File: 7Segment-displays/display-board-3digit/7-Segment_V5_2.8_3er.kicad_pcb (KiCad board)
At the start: 2 copper layers, 47.8 x 10.7 mm, 5 parts, among them J1 Conn_02x08_Odd_Even, U1 7Segment 3 digit common catho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

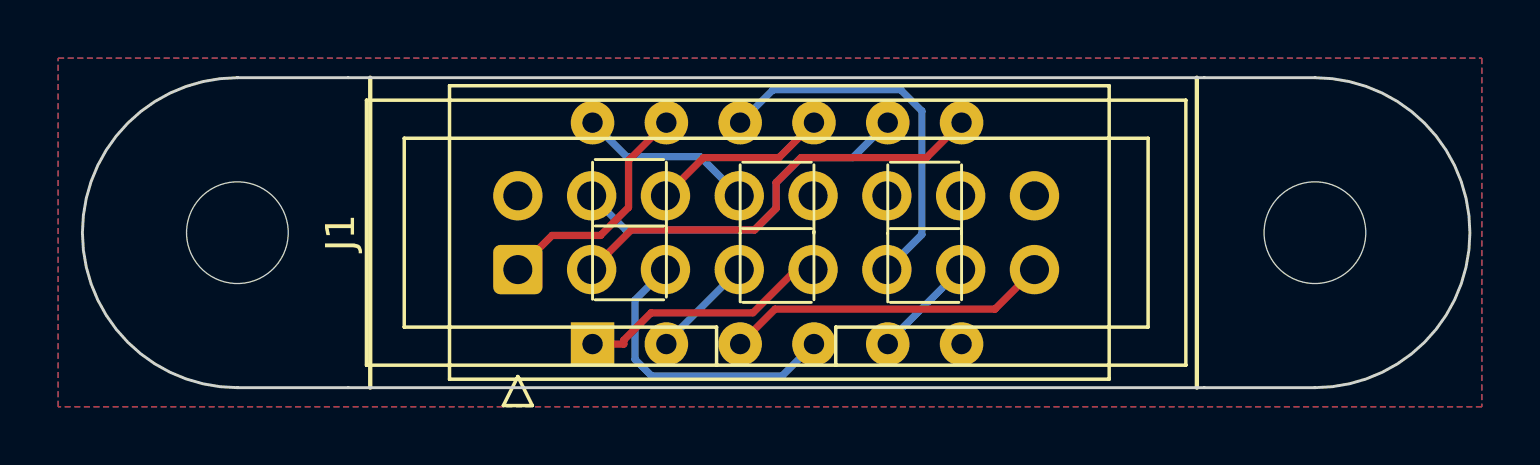
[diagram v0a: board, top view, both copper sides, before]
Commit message: update 4/5/6 digit schematic and pcb to MF lib, add 3 digit to lib
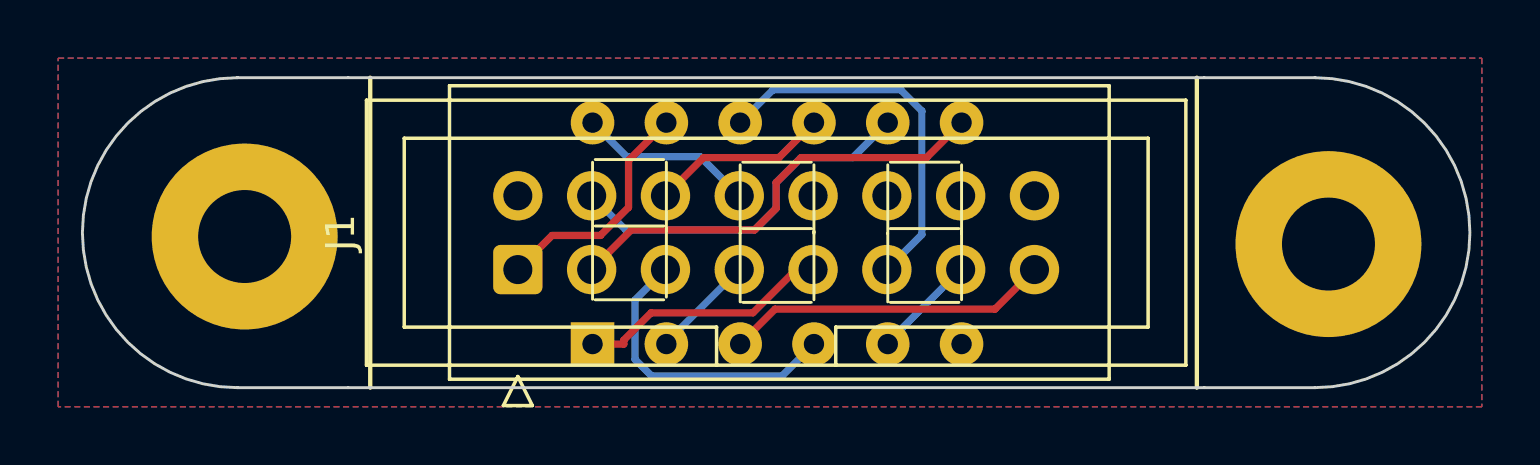
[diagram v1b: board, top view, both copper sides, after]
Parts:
- removed REF1: MountingHole_3.5mm1, MountingHole:MountingHole_3.5mm
- removed REF2: MountingHole_3.5mm2, MountingHole:MountingHole_3.5mm
- added H1: MountingHole, MountingHole:MountingHole_3.2mm_M3_Pad, F.Cu at (90.4, 64.1)
- added H2: MountingHole, MountingHole:MountingHole_3.2mm_M3_Pad, F.Cu at (127.7, 64.4)
- G2: footprint Logo:MobiFlight1 -> MobiFlight:MobiFlight-Logo-Small
- U1: footprint Display_7Segment:STH_7_3 Digits_0.28_CC -> MobiFlight:STH_7_3 Digits_0.28_CC
- moved G2 3.69 mm to (96.3, 64.2)
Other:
- board text added: "MobiFlight Display System 2.8mm ${REVISION}"
- board text removed: "MobiFlight Display System 2.8mm V5.1"
